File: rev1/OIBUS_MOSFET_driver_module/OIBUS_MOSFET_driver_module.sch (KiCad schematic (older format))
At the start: 24 parts, among them T2 DMG6402LVT, U1 TLP291, U2 TLP291, U3 TLP291, U4 TLP291, U5 TLP291, U6 TLP291, U7 TLP291, U8 TLP291

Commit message: captured schematics, pending review
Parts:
- removed R? (x7): R, symbol Device:R
- added C1, C2: 100u Elko, symbol Device:CP
- added C10, C11, C12, C13, C5, C6, C9: 100n, symbol Device:C_Small
- added C14: 1u, symbol Device:C_Small
- added C15: 10n, symbol Device:C_Small
- added C7, C8: 10p, symbol Device:C_Small
- added D1, D11, D13, D15, D18, D5, D7, D9: D, symbol Device:D
- added D10, D12, D14, D16, D2, D6, D8: D_Zener, symbol Device:D_Zener
- added D17: D_TVS_x2_AAC, symbol Device:D_TVS_x2_AAC
- added J1: SWD, symbol Connector:Conn_01x06_Male
- added J10, J11, J4, J5, J6, J7, J8, J9: +, symbol Connector:Screw_Terminal_01x02
- added J2: UART, symbol Connector:Conn_01x02_Male
- added J3: 5V - 24V, Molex Ultrafit, symbol Connector:Conn_01x02_Female
- added JP1, JP2: SolderJumper_3_Open, symbol Jumper:SolderJumper_3_Open
- added JP10, JP11, JP12, JP13, JP14, JP15, JP16, JP17, JP18, JP19, JP20, JP3, JP4, JP5, JP6, JP7, JP8, JP9: SolderJumper_2_Open, symbol Jumper:SolderJumper_2_Open
- added JP21, JP22, JP23, JP24, JP25, JP26, JP27, JP28, JP29: 0 OHM, symbol Jumper:SolderJumper_2_Open
- added L1: 10uH, symbol pspice:INDUCTOR
- added LED1, LED3, LED4, LED5, LED6, LED7, LED8, LED9: LED, symbol Device:LED
- added R1, R11, R13, R15, R5, R7, R9: 4K7, symbol Device:R
- added R10, R12, R14, R16, R2, R6, R8: 18K, symbol Device:R
- added R18, R19, R20, R21, R22, R23, R24: 1K5, symbol Device:R
- added R25, R26: 60, symbol Device:R_Small
- added R27: 330, symbol Device:R
- added T1, T3, T4, T5, T6, T7, T8: DMG6402LVT, symbol DMG6402LVT:DMG6402LVT
- added U10: STM32F303CCTx, Package_QFP:LQFP-48_7x7mm_P0.5mm, symbol MCU_ST_STM32F3:STM32F303CCTx
- added U9: TCAN330, symbol Interface_CAN_LIN:TCAN330
- added Y1: 16MHz, symbol Device:Crystal
- R17: renamed from R?; value R -> 1K5
- gave numbers to parts that had none: 5
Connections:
- net labels added: +3V3, ADC0, ADC1, ADC2, ADC3, ADC4, ADC5, CANH, CANL, GND, GPIO1, GPIO2, GPIO3, GPIO4, GateT1, GateT2, GateT3, GateT4, GateT5, GateT6, GateT7, GateT8, In1, In2, In3, In4, In5, In6, In7, In8, Rx, SWDCLK, SWDIO, SWDSWO, Tx, VBACKUP, VBUS, Vopto, ~RESET
- net labels removed: E2, GNDD, OD2
- wire segments 24 -> 477
- no-connect marks 0 -> 7
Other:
- note added: "Optional \nCAN Termination"
- note added: "STM32"
- note added: "SWCLK-JTCK"
- note added: "SWDIO-JTMS"
- note added: "Transient Voltage \nSuppression\n(put close to can connector)"
- note added: "USART3_RX"
- note added: "USART3_TX"
- moved on the sheet: D3, D4, H1, H2, LED2, R17, R3, R4, T2, U1

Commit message: adding 2 more drivers, assigend footprints
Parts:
- removed Y1: 16MHz, symbol Device:Crystal
- added D19, D20: D, FM4004W-W:DIOM5025X231N, symbol Device:D
- added D21, D22: D_Zener, TO_SOT_Packages_SMD:SOT-23, symbol Device:D_Zener
- added H3, H4, H5, H6: MountingHole_Pad, Mounting_Holes:MountingHole_3.2mm_M3_DIN965_Pad, symbol Mechanical:MountingHole_Pad
- added J12, J13: +, CTB93HE_2:SHDR2W80P0X381_1X2_900X920X725P, symbol Connector:Screw_Terminal_01x02
- added LED10, LED11: LED, LEDs:LED_0603, symbol Device:LED
- added R28, R29: 4K7, Resistors_SMD:R_0603, symbol Device:R
- added R30, R31: 18K, Resistors_SMD:R_0603, symbol Device:R
- added R32, R33: 1K5, Resistors_SMD:R_0603, symbol Device:R
- added T10, T9: DMG6402LVT, DMG6602SVT-7:SOT95P280X90-6N, symbol DMG6402LVT:DMG6402LVT
- added U11, U12: TLP291, Package_DIP:SMDIP-4_W7.62mm, symbol Isolator:TLP291
- added Y1: 16M, Crystals:Crystal_SMD_SeikoEpson_FA238-4pin_3.2x2.5mm, symbol Device:Crystal_GND24_Small
- C1, C2: footprint (none) -> Capacitors_SMD:CP_Elec_6.3x7.7
- C10, C11, C12, C13, C14, C15, C5, C6, C7, C8, C9: footprint (none) -> Capacitors_SMD:C_0603
- D1, D11, D13, D15, D3, D5, D7, D9: footprint (none) -> FM4004W-W:DIOM5025X231N
- D10, D12, D14, D16, D2, D4, D6, D8: footprint (none) -> TO_SOT_Packages_SMD:SOT-23
- D17: footprint (none) -> TO_SOT_Packages_SMD:SOT-323_SC-70
- D18: footprint (none) -> Diodes_SMD:D_SOD-123
- H1, H2: footprint (none) -> lib_fp_global:SAMTEC_SSQ-126-22-G-D
- J1: footprint (none) -> Pin_Headers:Pin_Header_Angled_1x06_Pitch2.54mm
- J10, J11, J4, J5, J6, J7, J8, J9: footprint (none) -> CTB93HE_2:SHDR2W80P0X381_1X2_900X920X725P
- J2: footprint (none) -> Pin_Headers:Pin_Header_Angled_1x02_Pitch2.54mm
- J3: footprint (none) -> 172310-1202:172310-1202
- JP1, JP2: footprint (none) -> Jumper:SolderJumper-3_P1.3mm_Open_RoundedPad1.0x1.5mm
- JP10, JP11, JP12, JP13, JP14, JP15, JP16, JP17, JP18, JP19, JP20, JP21, JP22, JP23, JP24, JP25, JP26, JP27, JP28, JP29, JP3, JP4, JP5, JP6, JP7, JP8, JP9, R1, R10, R11, R12, R13, R14, R15, R16, R17, R18, R19, R2, R20, R21, R22, R23, R24, R27, R3, R4, R5, R6, R7, R8, R9: footprint (none) -> Resistors_SMD:R_0603
- L1: footprint (none) -> Inductors_SMD:L_0805
- LED1, LED2, LED3, LED4, LED5, LED6, LED7, LED8, LED9: footprint (none) -> LEDs:LED_0603
- R25, R26: footprint (none) -> Resistors_SMD:R_1206
- T1, T2, T3, T4, T5, T6, T7, T8: footprint (none) -> DMG6602SVT-7:SOT95P280X90-6N
- U9: footprint (none) -> TO_SOT_Packages_SMD:SOT-23-8
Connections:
- net labels added: GateT10, GateT9, In10, In9
- wire segments 477 -> 563
- no-connect marks 7 -> 63
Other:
- moved on the sheet: C1, D1, D10, D11, D12, D13, D14, D15, D16, D18, D2, D3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

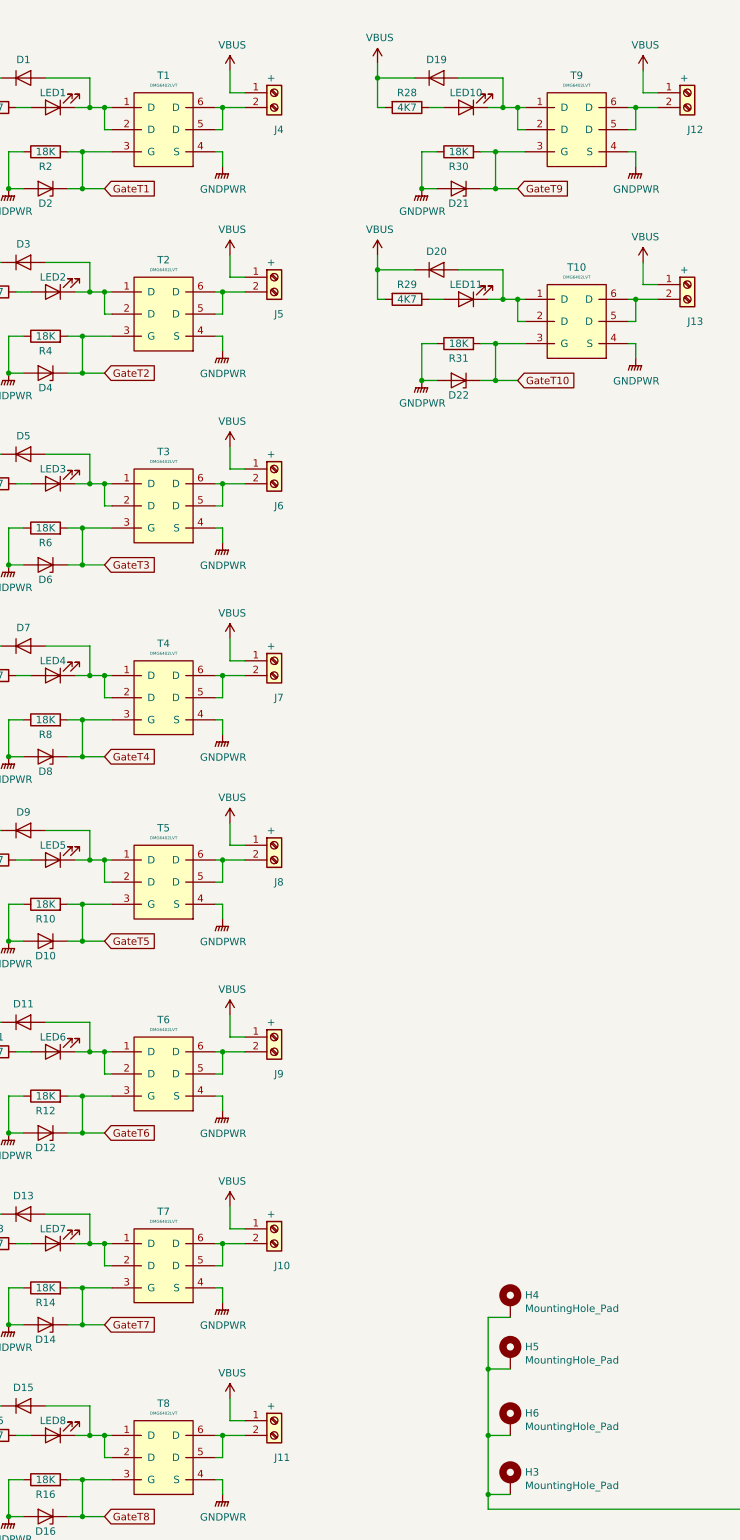
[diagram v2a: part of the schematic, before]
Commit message: adding power lanes
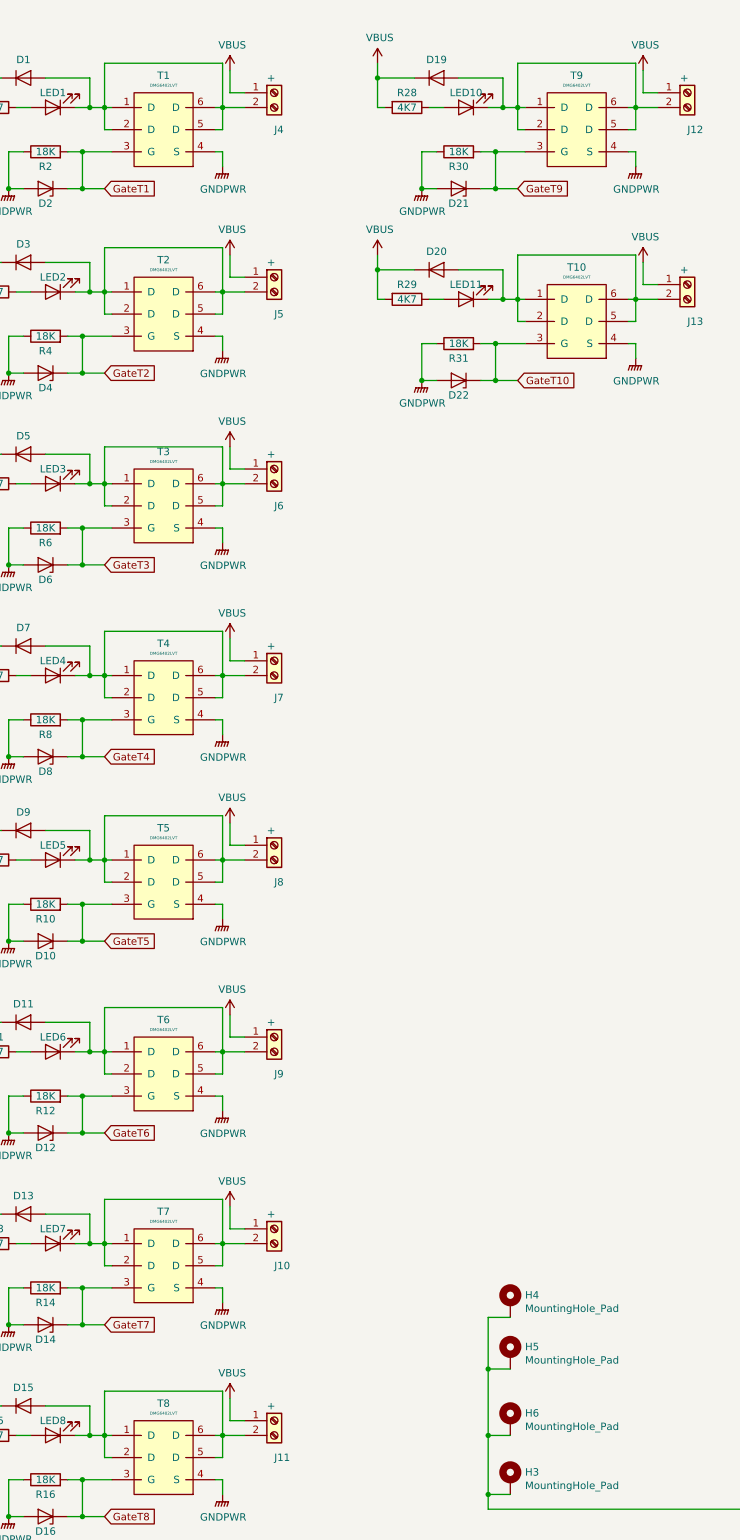
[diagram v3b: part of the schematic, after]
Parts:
- J3: footprint 172310-1202:172310-1202 -> 172310-1202:MOLEX_172310-1202
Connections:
- net at D3.2 (A), LED2.1 (K), T2.1 (D)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: now also J5.2 (Pin_2), T2.5 (D), T2.6 (D)
- net at J4.2 (Pin_2), T1.5 (D), T1.6 (D): now also D1.2 (A), LED1.1 (K), T1.1 (D), T1.2 (D)
- net at D7.2 (A), LED4.1 (K), T4.1 (D)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: now also J7.2 (Pin_2), T4.5 (D), T4.6 (D)
- net at D5.2 (A), LED3.1 (K), T3.1 (D)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: now also J6.2 (Pin_2), T3.5 (D), T3.6 (D)
- net at D11.2 (A), LED6.1 (K), T6.1 (D)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: now also J9.2 (Pin_2), T6.5 (D), T6.6 (D)
- net at D9.2 (A), LED5.1 (K), T5.1 (D)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: now also J8.2 (Pin_2), T5.5 (D), T5.6 (D)
- net at D15.2 (A), LED8.1 (K), T8.1 (D)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: now also J11.2 (Pin_2), T8.5 (D), T8.6 (D)
- net at D13.2 (A), LED7.1 (K), T7.1 (D)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: now also J10.2 (Pin_2), T7.5 (D), T7.6 (D)
- net at D20.2 (A), LED11.1 (K), T10.1 (D)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: now also J13.2 (Pin_2), T10.5 (D), T10.6 (D)
- net at D19.2 (A), LED10.1 (K), T9.1 (D)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: now also J12.2 (Pin_2), T9.5 (D), T9.6 (D)
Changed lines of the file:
@@
 F 0 "J3" H 10628 10176 50  0000 L CNN
 F 1 "5V - 24V, Molex Ultrafit" H 10550 10300 50  0000 L CNN
-F 2 "172310-1202:172310-1202" H 10600 10200 50  0001 C CNN
+F 2 "172310-1202:MOLEX_172310-1202" H 10600 10200 50  0001 C CNN
 F 3 "~" H 10600 10200 50  0001 C CNN
 	1    10600 10200
@@
 Wire Wire Line
 	10100 10650 10100 10800
+Wire Wire Line
+	5250 1150 5250 850
+Wire Wire Line
+	5250 850  6050 850
+Wire Wire Line
+	6050 850  6050 1150
+Wire Wire Line
+	6050 2400 6050 2100
+Wire Wire Line
+	6050 2100 5250 2100
+Wire Wire Line
+	5250 2100 5250 2400
+Wire Wire Line
+	5250 3700 5250 3450
+Wire Wire Line
+	5250 3450 6050 3450
+Wire Wire Line
+	6050 3450 6050 3700
+Wire Wire Line
+	6050 5000 6050 4700
+Wire Wire Line
+	6050 4700 5250 4700
+Wire Wire Line
+	5250 4700 5250 5000
+Wire Wire Line
+	6050 6250 6050 5950
+Wire Wire Line
+	6050 5950 5250 5950
+Wire Wire Line
+	5250 5950 5250 6250
+Wire Wire Line
+	6050 7550 6050 7250
+Wire Wire Line
+	6050 7250 5250 7250
+Wire Wire Line
+	5250 7250 5250 7550
+Wire Wire Line
+	6050 8850 6050 8550
+Wire Wire Line
+	6050 8550 5250 8550
+Wire Wire Line
+	5250 8550 5250 8850
+Wire Wire Line
+	6050 10150 6050 9850
+Wire Wire Line
+	6050 9850 5250 9850
+Wire Wire Line
+	5250 9850 5250 10150
+Wire Wire Line
+	8850 2450 8850 2150
+Wire Wire Line
+	8850 2150 8050 2150
+Wire Wire Line
+	8050 2150 8050 2450
+Wire Wire Line
+	8850 1150 8850 850
+Wire Wire Line
+	8850 850  8050 850
+Wire Wire Line
+	8050 850  8050 1150
 $EndSCHEMATC

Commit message: pcb layout completed and ready for review
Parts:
- removed JP13, JP14, JP15, JP16, JP17, JP18, JP19, JP20, JP4, JP6, JP7, JP8: SolderJumper_2_Open, Resistors_SMD:R_0603, symbol Jumper:SolderJumper_2_Open
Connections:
- net ADC2 is gone; now on net ADC1: JP5.2 (B), U10.14 (PA4)
- net ADC1: no longer U10.12 (PA2)
- net GND: now also H2.29 (GND), H2.30 (GND), H3.1, H4.1, H5.1, H6.1, JP28.1 (A)
- net GNDPWR: no longer H3.1, H4.1, H5.1, H6.1
- net Tx: now also JP1.3 (B); no longer JP1.1 (A)
- net at H1.39 (COMM_TX): now also JP1.1 (A); no longer JP1.3 (B)
- net ADC3: no longer names the net of U10.15 (PA5)
- net ADC4: no longer names the net of U10.16 (PA6)
- net ADC5: no longer names the net of U10.17 (PA7)
- no-connect marks 63 -> 75
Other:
- moved on the sheet: JP1
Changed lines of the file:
@@
 $EndComp
 Wire Wire Line
-	10100 10500 10100 10650
-Wire Wire Line
 	10400 10300 10300 10300
 Wire Wire Line
@@
 	14800 6050 14650 6050
 Wire Wire Line
-	14650 6150 14800 6150
+	14650 6150 14700 6150
 Wire Wire Line
 	14800 6150 14800 6050
@@
 Text GLabel 11900 7850 2    50   Input ~ 0
 ADC0
-Text GLabel 11900 7950 2    50   Input ~ 0
-ADC1
 Text GLabel 11900 8050 2    50   Input ~ 0
-ADC2
-Text GLabel 11900 8150 2    50   Input ~ 0
-ADC3
-Text GLabel 11900 8250 2    50   Input ~ 0
-ADC4
-Text GLabel 11900 8350 2    50   Input ~ 0
-ADC5
+ADC1
 $Comp
 L Jumper:SolderJumper_2_Open JP3
@@
 $EndComp
 $Comp
-L Jumper:SolderJumper_2_Open JP4
-U 1 1 5D96E097
-P 11750 7950
-F 0 "JP4" H 11700 7900 12  0000 C CNN
-F 1 "SolderJumper_2_Open" H 11750 8064 50  0001 C CNN
-F 2 "Resistors_SMD:R_0603" H 11750 7950 50  0001 C CNN
-F 3 "~" H 11750 7950 50  0001 C CNN
-	1    11750 7950
-	1    0    0    -1
-$EndComp
-$Comp
 L Jumper:SolderJumper_2_Open JP5
 U 1 1 5D96E185
@@
 	1    0    0    -1
 $EndComp
-$Comp
-L Jumper:SolderJumper_2_Open JP6
-U 1 1 5D96E273
-P 11750 8150
-F 0 "JP6" H 11700 8100 12  0000 C CNN
-F 1 "SolderJumper_2_Open" H 11750 8264 50  0001 C CNN
-F 2 "Resistors_SMD:R_0603" H 11750 8150 50  0001 C CNN
-F 3 "~" H 11750 8150 50  0001 C CNN
-	1    11750 8150
-	1    0    0    -1
-$EndComp
-$Comp
-L Jumper:SolderJumper_2_Open JP7
-U 1 1 5D96E364
-P 11750 8250
-F 0 "JP7" H 11700 8200 12  0000 C CNN
-F 1 "SolderJumper_2_Open" H 11750 8364 50  0001 C CNN
-F 2 "Resistors_SMD:R_0603" H 11750 8250 50  0001 C CNN
-F 3 "~" H 11750 8250 50  0001 C CNN
-	1    11750 8250
-	1    0    0    -1
-$EndComp
-$Comp
-L Jumper:SolderJumper_2_Open JP8
-U 1 1 5D96E456
-P 11750 8350
-F 0 "JP8" H 11700 8300 12  0000 C CNN
-F 1 "SolderJumper_2_Open" H 11750 8464 50  0001 C CNN
-F 2 "Resistors_SMD:R_0603" H 11750 8350 50  0001 C CNN
-F 3 "~" H 11750 8350 50  0001 C CNN
-	1    11750 8350
-	1    0    0    -1
-$EndComp
 Text GLabel 15100 3200 2    50   Input ~ 0
 ADC0
-Text GLabel 15100 3300 2    50   Input ~ 0
-ADC1
 Text GLabel 15100 3500 2    50   Input ~ 0
-ADC2
-Text GLabel 15100 3600 2    50   Input ~ 0
-ADC3
-Text GLabel 15100 3700 2    50   Input ~ 0
-ADC4
-Text GLabel 15100 3800 2    50   Input ~ 0
-ADC5
+ADC1
 Wire Wire Line
 	15100 3200 14750 3200
 Wire Wire Line
-	15100 3300 14750 3300
-Wire Wire Line
 	14750 3500 15100 3500
 Wire Wire Line
-	15100 3600 14750 3600
-Wire Wire Line
-	14750 3700 15100 3700
-Wire Wire Line
-	15100 3800 14750 3800
-Wire Wire Line
 	13300 4500 13450 4500
 Wire Wire Line
@@
 Wire Wire Line
 	10850 1050 11750 1050
-Text GLabel 12100 7050 2    50   Input ~ 0
+Text GLabel 12200 6950 2    50   Input ~ 0
 Tx
 Text GLabel 12100 7150 2    50   Input ~ 0
 Rx
 $Comp
-L Jumper:SolderJumper_3_Open JP1
-U 1 1 5E08FA34
-P 11850 7050
-F 0 "JP1" H 11700 6950 50  0000 C CNN
-F 1 "SolderJumper_3_Open" H 11850 7253 50  0001 C CNN
-F 2 "Jumper:SolderJumper-3_P1.3mm_Open_RoundedPad1.0x1.5mm" H 11850 7050 50  0001 C CNN
-F 3 "~" H 11850 7050 50  0001 C CNN
-	1    11850 7050
-	-1   0    0    1
-$EndComp
-$Comp
 L Jumper:SolderJumper_3_Open JP2
 U 1 1 5E09018A
@@
 	11750 7500 11800 7500
 Wire Wire Line
-	12100 7050 12050 7050
-Wire Wire Line
 	12100 7150 12050 7150
 Wire Wire Line
-	11650 7050 11600 7050
-Wire Wire Line
 	11650 7150 11600 7150
 $Comp
@@
 $EndComp
 Wire Wire Line
-	11850 6900 11850 6800
-Wire Wire Line
-	11850 6800 12400 6800
-Wire Wire Line
-	12400 6800 12400 7050
-Wire Wire Line
 	12400 7150 12400 7400
 Wire Wire Line
@@
 Wire Wire Line
 	11850 7400 11850 7300
-Text GLabel 10200 6350 0    50   Input ~ 0
-In3
-Text GLabel 10200 6250 0    50   Input ~ 0
-In4
-Text GLabel 10200 6150 0    50   Input ~ 0
-In5
-Text GLabel 10200 6050 0    50   Input ~ 0
-In6
-Text GLabel 10200 5950 0    50   Input ~ 0
-In7
-Text GLabel 10200 5850 0    50   Input ~ 0
-In8
-$Comp
-L Jumper:SolderJumper_2_Open JP15
-U 1 1 5E219003
-P 10350 6350
-F 0 "JP15" H 10300 6300 12  0000 C CNN
-F 1 "SolderJumper_2_Open" H 10350 6464 50  0001 C CNN
-F 2 "Resistors_SMD:R_0603" H 10350 6350 50  0001 C CNN
-F 3 "~" H 10350 6350 50  0001 C CNN
-	1    10350 6350
-	-1   0    0    1
-$EndComp
-$Comp
-L Jumper:SolderJumper_2_Open JP16
-U 1 1 5E21900A
-P 10350 6250
-F 0 "JP16" H 10300 6200 12  0000 C CNN
-F 1 "SolderJumper_2_Open" H 10350 6364 50  0001 C CNN
-F 2 "Resistors_SMD:R_0603" H 10350 6250 50  0001 C CNN
-F 3 "~" H 10350 6250 50  0001 C CNN
-	1    10350 6250
-	-1   0    0    1
-$EndComp
-$Comp
-L Jumper:SolderJumper_2_Open JP17
-U 1 1 5E219011
-P 10350 6150
-F 0 "JP17" H 10300 6100 12  0000 C CNN
-F 1 "SolderJumper_2_Open" H 10350 6264 50  0001 C CNN
-F 2 "Resistors_SMD:R_0603" H 10350 6150 50  0001 C CNN
-F 3 "~" H 10350 6150 50  0001 C CNN
-	1    10350 6150
-	-1   0    0    1
-$EndComp
-$Comp
-L Jumper:SolderJumper_2_Open JP18
-U 1 1 5E219018
-P 10350 6050
-F 0 "JP18" H 10300 6000 12  0000 C CNN
-F 1 "SolderJumper_2_Open" H 10350 6164 50  0001 C CNN
-F 2 "Resistors_SMD:R_0603" H 10350 6050 50  0001 C CNN
-F 3 "~" H 10350 6050 50  0001 C CNN
-	1    10350 6050
-	-1   0    0    1
-$EndComp
-$Comp
-L Jumper:SolderJumper_2_Open JP19
-U 1 1 5E21901F
-P 10350 5950
-F 0 "JP19" H 10300 5900 12  0000 C CNN
-F 1 "SolderJumper_2_Open" H 10350 6064 50  0001 C CNN
-F 2 "Resistors_SMD:R_0603" H 10350 5950 50  0001 C CNN
-F 3 "~" H 10350 5950 50  0001 C CNN
-	1    10350 5950
-	-1   0    0    1
-$EndComp
-$Comp
-L Jumper:SolderJumper_2_Open JP20
-U 1 1 5E219026
-P 10350 5850
-F 0 "JP20" H 10300 5800 12  0000 C CNN
-F 1 "SolderJumper_2_Open" H 10350 5964 50  0001 C CNN
-F 2 "Resistors_SMD:R_0603" H 10350 5850 50  0001 C CNN
-F 3 "~" H 10350 5850 50  0001 C CNN
-	1    10350 5850
-	-1   0    0    1
-$EndComp
-$Comp
-L Jumper:SolderJumper_2_Open JP13
-U 1 1 5E2FB309
-P 10350 6550
-F 0 "JP13" H 10300 6500 12  0000 C CNN
-F 1 "SolderJumper_2_Open" H 10350 6664 50  0001 C CNN
-F 2 "Resistors_SMD:R_0603" H 10350 6550 50  0001 C CNN
-F 3 "~" H 10350 6550 50  0001 C CNN
-	1    10350 6550
-	-1   0    0    1
-$EndComp
-$Comp
-L Jumper:SolderJumper_2_Open JP14
-U 1 1 5E2FB310
-P 10350 6450
-F 0 "JP14" H 10300 6400 12  0000 C CNN
-F 1 "SolderJumper_2_Open" H 10350 6564 50  0001 C CNN
-F 2 "Resistors_SMD:R_0603" H 10350 6450 50  0001 C CNN
-F 3 "~" H 10350 6450 50  0001 C CNN
-	1    10350 6450
-	-1   0    0    1
-$EndComp
-Text GLabel 10200 6550 0    50   Input ~ 0
-In1
-Text GLabel 10200 6450 0    50   Input ~ 0
-In2
 Text GLabel 13350 3500 0    50   Input ~ 0
 GPIO1
@@
 	7850 10550 8000 10550
 Connection ~ 7850 10150
-Wire Wire Line
-	7850 10550 7850 10650
-Wire Wire Line
-	7850 10650 10100 10650
 Connection ~ 7850 10550
-Connection ~ 10100 10650
-Wire Wire Line
-	10100 10650 10100 10800
 Wire Wire Line
 	5250 1150 5250 850
@@
 Wire Wire Line
 	8050 850  8050 1150
+Wire Wire Line
+	10100 10500 10100 10800
+$Comp
+L power:GND #PWR0102
+U 1 1 5C1EFFE1
+P 7850 10850
+F 0 "#PWR0102" H 7850 10600 50  0001 C CNN
+F 1 "GND" H 7855 10677 50  0000 C CNN
+F 2 "" H 7850 10850 50  0001 C CNN
+F 3 "" H 7850 10850 50  0001 C CNN
+	1    7850 10850
+	1    0    0    -1
+$EndComp
+Wire Wire Line
+	7850 10550 7850 10850
+Wire Wire Line
+	14700 6250 14700 6150
+Connection ~ 14700 6150
+Wire Wire Line
+	14700 6150 14800 6150
+NoConn ~ 10500 6550
+NoConn ~ 10500 6450
+NoConn ~ 10500 6350
+NoConn ~ 10500 6250
+NoConn ~ 10500 6150
+NoConn ~ 10500 6050
+NoConn ~ 10500 5950
+NoConn ~ 10500 5850
+NoConn ~ 14750 3700
+NoConn ~ 14750 3800
+$Comp
+L Jumper:SolderJumper_3_Open JP1
+U 1 1 5E08FA34
+P 12000 6950
+F 0 "JP1" H 11850 6850 50  0000 C CNN
+F 1 "SolderJumper_3_Open" H 12000 7153 50  0001 C CNN
+F 2 "Jumper:SolderJumper-3_P1.3mm_Open_RoundedPad1.0x1.5mm" H 12000 6950 50  0001 C CNN
+F 3 "~" H 12000 6950 50  0001 C CNN
+	1    12000 6950
+	1    0    0    -1
+$EndComp
+Wire Wire Line
+	11800 6950 11750 6950
+Wire Wire Line
+	11750 6950 11750 7050
+Wire Wire Line
+	11600 7050 11750 7050
+Wire Wire Line
+	12400 7050 12100 7050
+Wire Wire Line
+	12100 7050 12100 7100
+Wire Wire Line
+	12100 7100 12000 7100
+NoConn ~ 14750 3300
+NoConn ~ 14750 3600
 $EndSCHEMATC
